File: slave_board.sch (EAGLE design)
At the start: 170 parts, among them IC1 NCP1117ST50T3G, IC2 NCP1117ST50T3G, IC3 ATMEGA2560-16AU, J11 1935161, J17 RJ45, J22 RJ45, J3 1935161, J6 1935161, K1 ORWH-SH-112D1F, Q1 PHB45NQ15T, Q2 PHB45NQ15T, Q3 BSS138L, Q5 BSS138L, Q7 PHB45NQ15T, Q8 IRFR9024TRPBF, U1 VNQ5E160KTR-E, U3 INA213AIDCKT, U4 VNH7070ASTR, U5 VNH7070ASTR, U6 VNQ5E160KTR-E, U7 INA213AIDCKT, Y1 ABLS-16.000MHZ-B4-T

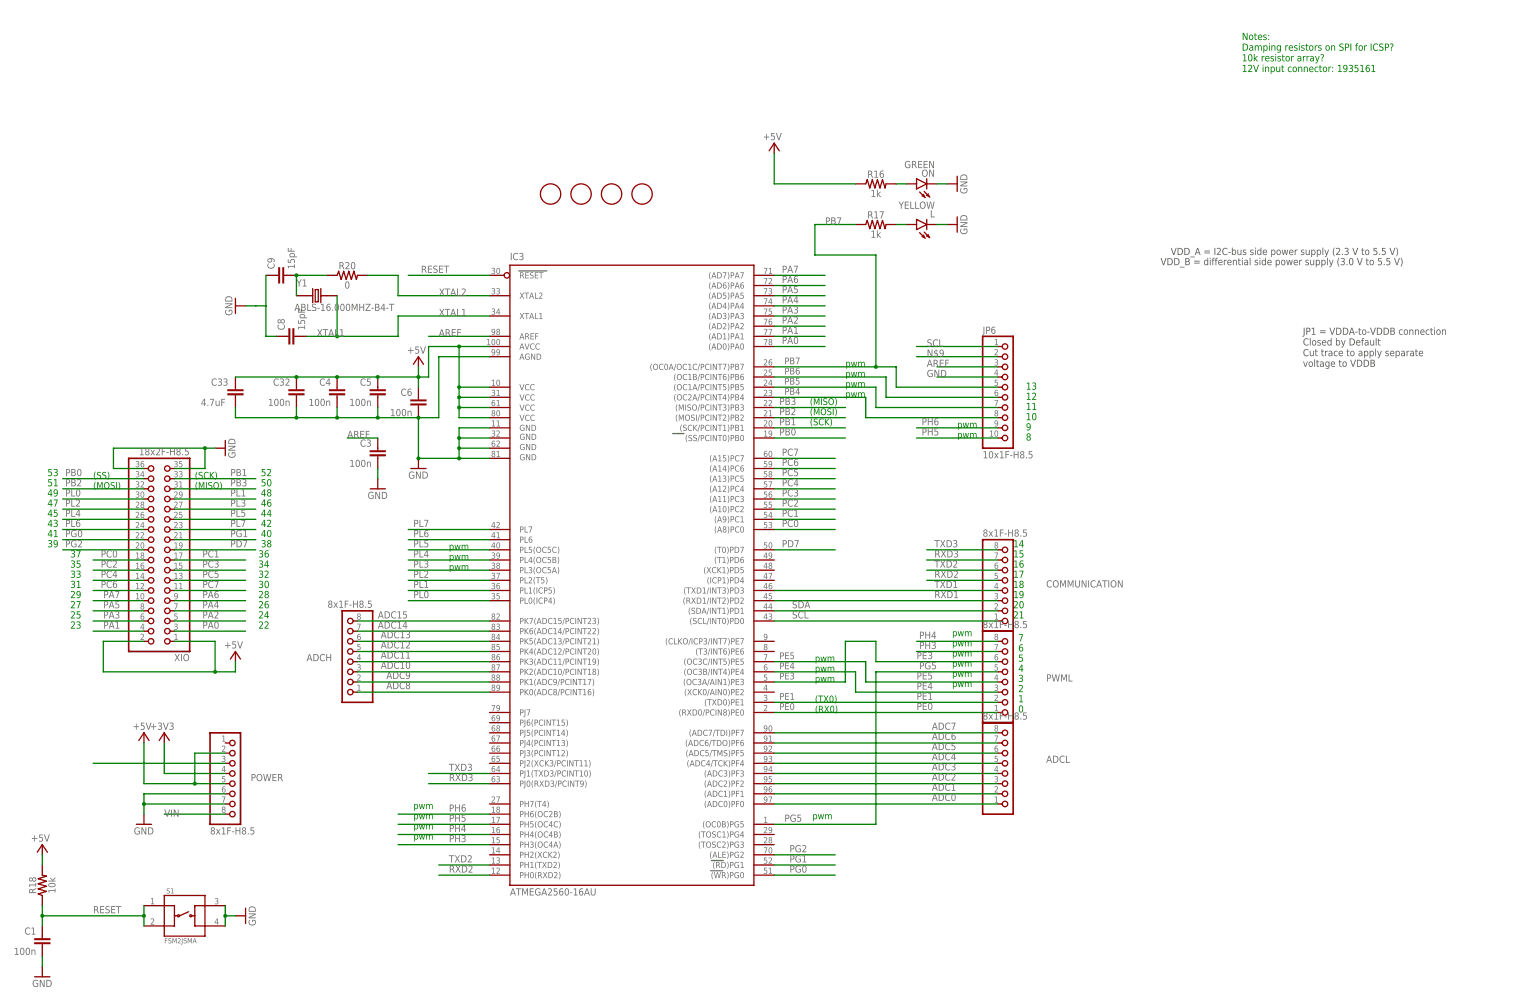
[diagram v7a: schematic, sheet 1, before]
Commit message: Wired microcontroller
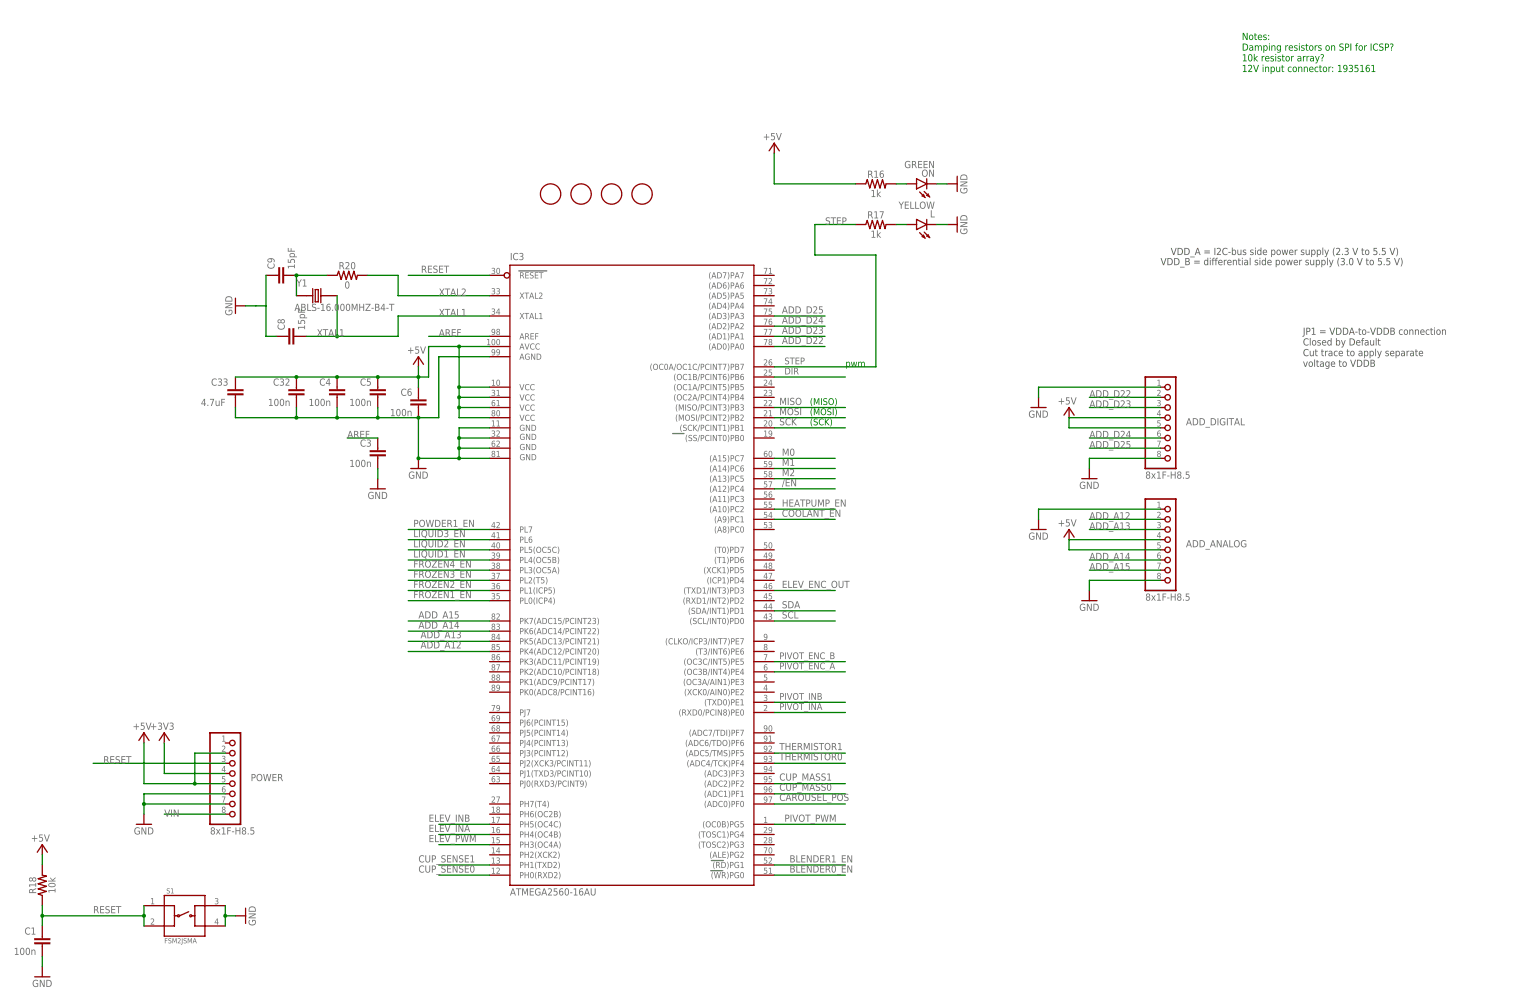
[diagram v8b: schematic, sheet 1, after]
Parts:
- removed ADCH, ADCL, COMMUNICATION, PWML: 8x1F-H8.5, SmartPrj:PINHD-1X8
- removed JP6: 10x1F-H8.5, SmartPrj:PINHD-1X10_ARD
- removed XIO: 18x2F-H8.5, SmartPrj:PINHD-2X18
- added ADD_ANALOG, ADD_DIGITAL: 8x1F-H8.5, SmartPrj:PINHD-1X8
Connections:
- removed net ADC0: ADCL.1, IC3.(ADC0)PF0
- removed net ADC1: ADCL.2, IC3.(ADC1)PF1
- removed net ADC10: ADCH.3, IC3.PK2(ADC10/PCINT18)
- removed net ADC11: ADCH.4, IC3.PK3(ADC11/PCINT19)
- removed net ADC12: ADCH.5, IC3.PK4(ADC12/PCINT20)
- removed net ADC13: ADCH.6, IC3.PK5(ADC13/PCINT21)
- removed net ADC14: ADCH.7, IC3.PK6(ADC14/PCINT22)
- removed net ADC15: ADCH.8, IC3.PK7(ADC15/PCINT23)
- removed net ADC2: ADCL.3, IC3.(ADC2)PF2
- removed net ADC3: ADCL.4, IC3.(ADC3)PF3
- removed net ADC4: ADCL.5, IC3.(ADC4/TCK)PF4
- removed net ADC5: ADCL.6, IC3.(ADC5/TMS)PF5
- removed net ADC6: ADCL.7, IC3.(ADC6/TDO)PF6
- removed net ADC7: ADCL.8, IC3.(ADC7/TDI)PF7
- removed net ADC8: ADCH.1, IC3.PK0(ADC8/PCINT16)
- removed net ADC9: ADCH.2, IC3.PK1(ADC9/PCINT17)
- removed net N$9: JP6.2
- removed net PA0: IC3.(AD0)PA0, XIO.3
- removed net PA1: IC3.(AD1)PA1, XIO.4
- removed net PA2: IC3.(AD2)PA2, XIO.5
- removed net PA3: IC3.(AD3)PA3, XIO.6
- removed net PA4: IC3.(AD4)PA4, XIO.7
- removed net PA5: IC3.(AD5)PA5, XIO.8
- removed net PA6: IC3.(AD6)PA6, XIO.9
- removed net PA7: IC3.(AD7)PA7, XIO.10
- removed net PB0: IC3.(SS/PCINT0)PB0, XIO.34
- removed net PB1: IC3.(SCK/PCINT1)PB1, ICSP1.3, TP9.1, XIO.33
- removed net PB2: IC3.(MOSI/PCINT2)PB2, ICSP1.4, TP7.1, XIO.32
- removed net PB3: IC3.(MISO/PCINT3)PB3, ICSP1.1, TP8.1, XIO.31
- removed net PB4: IC3.(OC2A/PCINT4)PB4, JP6.8
- removed net PB5: IC3.(OC1A/PCINT5)PB5, JP6.7
- removed net PB6: IC3.(OC1B/PCINT6)PB6, JP6.6
- removed net PB7: IC3.(OC0A/OC1C/PCINT7)PB7, JP6.5, R17.1
- removed net PC0: IC3.(A8)PC0, XIO.18
- removed net PC1: IC3.(A9)PC1, XIO.17
- removed net PC2: IC3.(A10)PC2, XIO.16
- removed net PC3: IC3.(A11)PC3, XIO.15
- removed net PC4: IC3.(A12)PC4, XIO.14
- removed net PC5: IC3.(A13)PC5, XIO.13
- removed net PC6: IC3.(A14)PC6, XIO.12
- removed net PC7: IC3.(A15)PC7, XIO.11
- removed net PD7: IC3.(T0)PD7, XIO.19
- removed net PE0: IC3.(RXD0/PCIN8)PE0, PWML.1
- removed net PE1: IC3.(TXD0)PE1, PWML.2
- removed net PE3: IC3.(OC3A/AIN1)PE3, PWML.6
- removed net PE4: IC3.(OC3B/INT4)PE4, PWML.3
- removed net PE5: IC3.(OC3C/INT5)PE5, PWML.4
- removed net PG0: IC3.(WR)PG0, XIO.22
- removed net PG1: IC3.(RD)PG1, XIO.21
- removed net PG2: IC3.(ALE)PG2, XIO.20
- removed net PG5: IC3.(OC0B)PG5, PWML.5
- removed net PH3: IC3.PH3(OC4A), PWML.7
- removed net PH4: IC3.PH4(OC4B), PWML.8
- removed net PH5: IC3.PH5(OC4C), JP6.10
- removed net PH6: IC3.PH6(OC2B), JP6.9
- removed net PL0: IC3.PL0(ICP4), XIO.30
- removed net PL1: IC3.PL1(ICP5), XIO.29
- removed net PL2: IC3.PL2(T5), XIO.28
- removed net PL3: IC3.PL3(OC5A), XIO.27
- removed net PL4: IC3.PL4(OC5B), XIO.26
- removed net PL5: IC3.PL5(OC5C), XIO.25
- removed net PL6: IC3.PL6, XIO.24
- removed net PL7: IC3.PL7, XIO.23
- removed net RXD1: COMMUNICATION.3, IC3.(RXD1/INT2)PD2
- removed net RXD2: COMMUNICATION.5, IC3.PH0(RXD2)
- removed net RXD3: COMMUNICATION.7, IC3.PJ0(RXD3/PCINT9)
- removed net TXD1: COMMUNICATION.4, IC3.(TXD1/INT3)PD3
- removed net TXD2: COMMUNICATION.6, IC3.PH1(TXD2)
- removed net TXD3: COMMUNICATION.8, IC3.PJ1(TXD3/PCINT10)
- removed net V-THERMISTOR0: C10.1, J4.2, R3.1
- removed net V-THERMISTOR1: C34.1, J1.2, R23.1
- new net ADD_A12: ADD_ANALOG.2, IC3.PK4(ADC12/PCINT20)
- new net ADD_A13: ADD_ANALOG.3, IC3.PK5(ADC13/PCINT21)
- new net ADD_A14: ADD_ANALOG.6, IC3.PK6(ADC14/PCINT22)
- new net ADD_A15: ADD_ANALOG.7, IC3.PK7(ADC15/PCINT23)
- new net ADD_D22: ADD_DIGITAL.2, IC3.(AD0)PA0
- new net ADD_D23: ADD_DIGITAL.3, IC3.(AD1)PA1
- new net ADD_D24: ADD_DIGITAL.6, IC3.(AD2)PA2
- new net ADD_D25: ADD_DIGITAL.7, IC3.(AD3)PA3
- new net MISO: IC3.(MISO/PCINT3)PB3, ICSP1.1, TP8.1
- new net MOSI: IC3.(MOSI/PCINT2)PB2, ICSP1.4, TP7.1
- new net SCK: IC3.(SCK/PCINT1)PB1, ICSP1.3, TP9.1
- new net THERMISTOR0: C10.1, IC3.(ADC4/TCK)PF4, J4.2, R3.1
- new net THERMISTOR1: C34.1, IC3.(ADC5/TMS)PF5, J1.2, R23.1
- net +5V: now also ADD_ANALOG.4, ADD_ANALOG.5, ADD_DIGITAL.4, ADD_DIGITAL.5; no longer XIO.1, XIO.2
- net /EN: now also IC3.(A12)PC4
- net AREF: no longer JP6.3
- net BLENDER0_EN: now also IC3.(WR)PG0
- net BLENDER1_EN: now also IC3.(RD)PG1
- net CAROUSEL_POS: now also IC3.(ADC0)PF0
- net COOLANT_EN: now also IC3.(A9)PC1
- net CUP_MASS0: now also IC3.(ADC1)PF1
- net CUP_MASS1: now also IC3.(ADC2)PF2
- net CUP_SENSE0: now also IC3.PH0(RXD2)
- net CUP_SENSE1: now also IC3.PH1(TXD2)
- net DIR: now also IC3.(OC1B/PCINT6)PB6
- net ELEV_ENC_OUT: now also IC3.(TXD1/INT3)PD3
- net ELEV_INA: now also IC3.PH4(OC4B)
- net ELEV_INB: now also IC3.PH5(OC4C)
- net ELEV_PWM: now also IC3.PH3(OC4A)
- net FROZEN1_EN: now also IC3.PL0(ICP4)
- net FROZEN2_EN: now also IC3.PL1(ICP5)
- net FROZEN3_EN: now also IC3.PL2(T5)
- net FROZEN4_EN: now also IC3.PL3(OC5A)
- net GND: now also ADD_ANALOG.1, ADD_ANALOG.8, ADD_DIGITAL.1, ADD_DIGITAL.8; no longer JP6.4, XIO.35, XIO.36
- net HEATPUMP_EN: now also IC3.(A10)PC2
- net LIQUID1_EN: now also IC3.PL4(OC5B)
- net LIQUID2_EN: now also IC3.PL5(OC5C)
- net LIQUID3_EN: now also IC3.PL6
- net M0: now also IC3.(A15)PC7
- net M1: now also IC3.(A14)PC6
- net M2: now also IC3.(A13)PC5
- net PIVOT_ENC_A: now also IC3.(OC3B/INT4)PE4
- net PIVOT_ENC_B: now also IC3.(OC3C/INT5)PE5
- net PIVOT_INA: now also IC3.(RXD0/PCIN8)PE0
- net PIVOT_INB: now also IC3.(TXD0)PE1
- net PIVOT_PWM: now also IC3.(OC0B)PG5
- net POWDER1_EN: now also IC3.PL7
- net SCL: no longer COMMUNICATION.1, JP6.1
- net SDA: no longer COMMUNICATION.2
- net STEP: now also IC3.(OC0A/OC1C/PCINT7)PB7, R17.1
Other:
- note removed: "(RX0)"
- note removed: "(SS)"
- note removed: "(TX0)"
- note removed: "0"
- note removed: "1"
- note removed: "10"
- note removed: "11"
- note removed: "12"
- note removed: "13"
- note removed: "14"
- note removed: "15"
- note removed: "16"
- note removed: "17"
- note removed: "18"
- note removed: "19"
- note removed: "2"
- note removed: "20"
- note removed: "21"
- note removed: "22"
- note removed: "23"
- note removed: "24"
- note removed: "25"
- note removed: "26"
- note removed: "27"
- note removed: "28"
- note removed: "29"
- note removed: "3"
- note removed: "30"
- note removed: "31"
- note removed: "32"
- note removed: "33"
- note removed: "34"
- note removed: "35"
- note removed: "36"
- note removed: "37"
- note removed: "38"
- note removed: "39"
- note removed: "4"
- note removed: "40"
- note removed: "41"
- note removed: "42"
- note removed: "43"
- note removed: "44"
- note removed: "45"
- note removed: "46"
- note removed: "47"
- note removed: "48"
- note removed: "49"
- note removed: "5"
- note removed: "50"
- note removed: "51"
- note removed: "52"
- note removed: "53"
- note removed: "6"
- note removed: "7"
- note removed: "8"
- note removed: "9"
